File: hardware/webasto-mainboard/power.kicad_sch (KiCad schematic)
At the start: 14 parts, among them U5 BD9G341EFJ

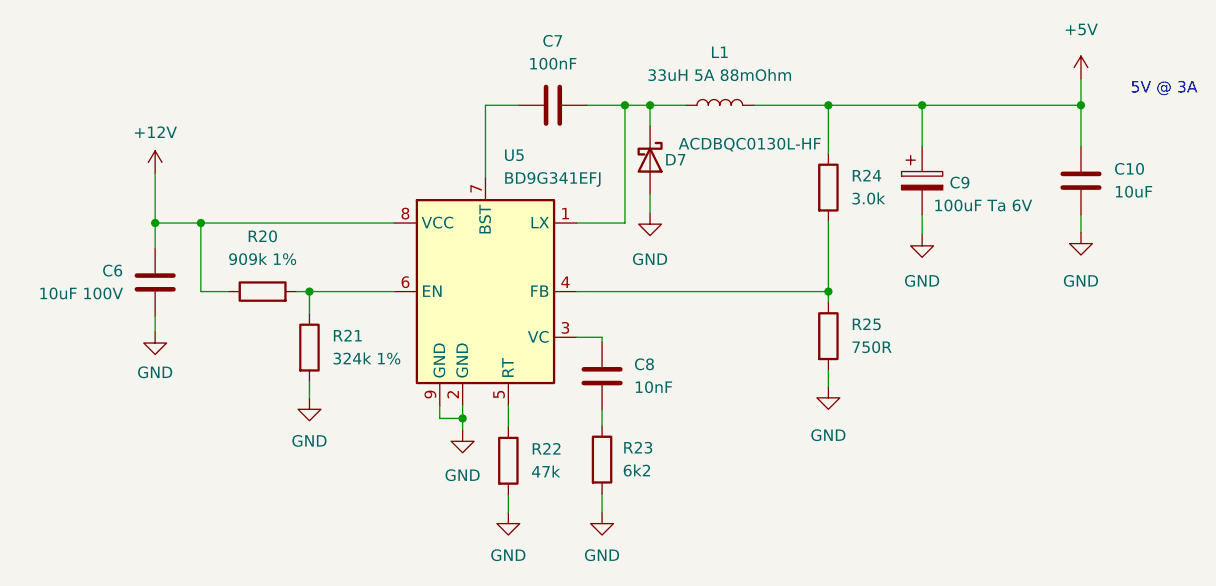
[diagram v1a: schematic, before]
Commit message: Added "USE_USB" input to choose console
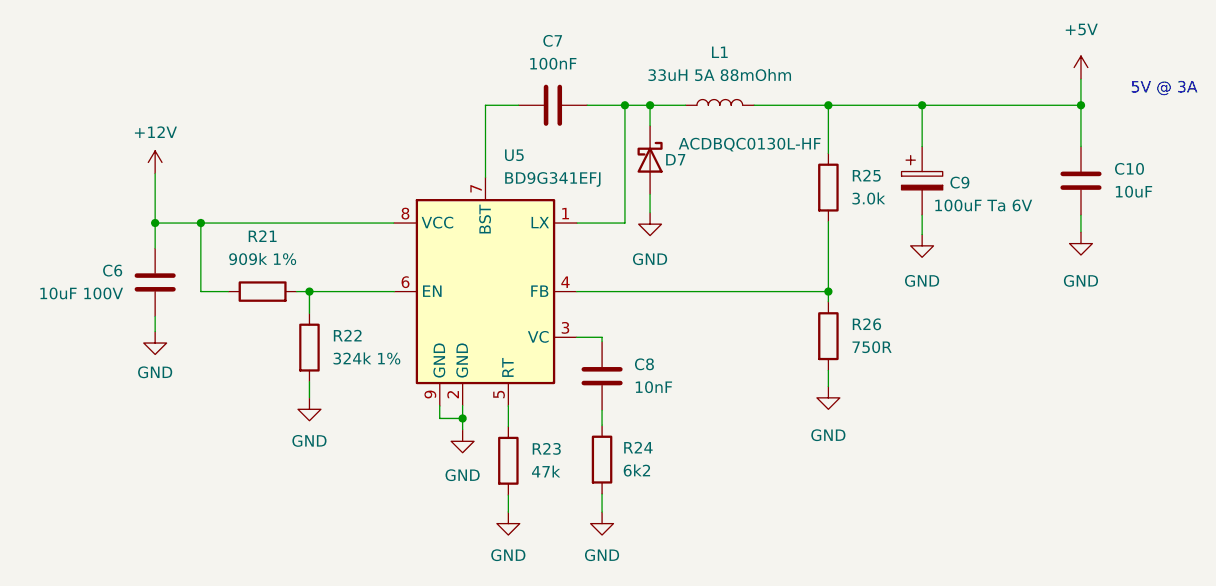
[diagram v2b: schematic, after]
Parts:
- renumbered R20 to R21, R21 to R22, R22 to R23, R23 to R24, R24 to R25, R25 to R26
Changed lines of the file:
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@@
   (symbol (lib_id "Device:R") (at 125.222 86.106 0) (unit 1)
     (in_bom yes) (on_board yes) (fields_autoplaced)
-    (property "Reference" "R21" (id 0) (at 127.762 84.8359 0)
+    (property "Reference" "R22" (id 0) (at 127.762 84.8359 0)
       (effects (font (size 1.27 1.27)) (justify left))
     )
@@
   (symbol (lib_id "power:GND") (at 210.947 73.279 0) (unit 1)
     (in_bom yes) (on_board yes) (fields_autoplaced)
-    (property "Reference" "#PWR056" (id 0) (at 210.947 79.629 0)
+    (property "Reference" "#PWR058" (id 0) (at 210.947 79.629 0)
       (effects (font (size 1.27 1.27)) hide)
     )
@@
   (symbol (lib_id "Device:R") (at 147.32 98.679 0) (unit 1)
     (in_bom yes) (on_board yes) (fields_autoplaced)
-    (property "Reference" "R22" (id 0) (at 149.86 97.4089 0)
+    (property "Reference" "R23" (id 0) (at 149.86 97.4089 0)
       (effects (font (size 1.27 1.27)) (justify left))
     )
@@
   (symbol (lib_id "power:GND") (at 163.068 71.12 0) (unit 1)
     (in_bom yes) (on_board yes) (fields_autoplaced)
-    (property "Reference" "#PWR052" (id 0) (at 163.068 77.47 0)
+    (property "Reference" "#PWR054" (id 0) (at 163.068 77.47 0)
       (effects (font (size 1.27 1.27)) hide)
     )
@@
   (symbol (lib_id "Device:R") (at 182.88 68.326 0) (unit 1)
     (in_bom yes) (on_board yes) (fields_autoplaced)
-    (property "Reference" "R24" (id 0) (at 185.42 67.0559 0)
+    (property "Reference" "R25" (id 0) (at 185.42 67.0559 0)
       (effects (font (size 1.27 1.27)) (justify left))
     )
@@
   (symbol (lib_id "power:GND") (at 193.294 73.533 0) (unit 1)
     (in_bom yes) (on_board yes) (fields_autoplaced)
-    (property "Reference" "#PWR054" (id 0) (at 193.294 79.883 0)
+    (property "Reference" "#PWR056" (id 0) (at 193.294 79.883 0)
       (effects (font (size 1.27 1.27)) hide)
     )
@@
   (symbol (lib_id "Device:R") (at 182.88 84.836 0) (unit 1)
     (in_bom yes) (on_board yes) (fields_autoplaced)
-    (property "Reference" "R25" (id 0) (at 185.42 83.5659 0)
+    (property "Reference" "R26" (id 0) (at 185.42 83.5659 0)
       (effects (font (size 1.27 1.27)) (justify left))
     )
@@
   (symbol (lib_id "power:GND") (at 108.077 84.328 0) (unit 1)
     (in_bom yes) (on_board yes) (fields_autoplaced)
-    (property "Reference" "#PWR047" (id 0) (at 108.077 90.678 0)
+    (property "Reference" "#PWR049" (id 0) (at 108.077 90.678 0)
       (effects (font (size 1.27 1.27)) hide)
     )
@@
   (symbol (lib_id "power:GND") (at 142.24 95.25 0) (unit 1)
     (in_bom yes) (on_board yes) (fields_autoplaced)
-    (property "Reference" "#PWR049" (id 0) (at 142.24 101.6 0)
+    (property "Reference" "#PWR051" (id 0) (at 142.24 101.6 0)
       (effects (font (size 1.27 1.27)) hide)
     )
@@
   (symbol (lib_id "power:GND") (at 125.222 91.694 0) (unit 1)
     (in_bom yes) (on_board yes) (fields_autoplaced)
-    (property "Reference" "#PWR048" (id 0) (at 125.222 98.044 0)
+    (property "Reference" "#PWR050" (id 0) (at 125.222 98.044 0)
       (effects (font (size 1.27 1.27)) hide)
     )
@@
   (symbol (lib_id "power:+12V") (at 108.077 66.802 0) (unit 1)
     (in_bom yes) (on_board yes) (fields_autoplaced)
-    (property "Reference" "#PWR046" (id 0) (at 108.077 70.612 0)
+    (property "Reference" "#PWR048" (id 0) (at 108.077 70.612 0)
       (effects (font (size 1.27 1.27)) hide)
     )
@@
   (symbol (lib_id "power:GND") (at 182.88 90.424 0) (unit 1)
     (in_bom yes) (on_board yes) (fields_autoplaced)
-    (property "Reference" "#PWR053" (id 0) (at 182.88 96.774 0)
+    (property "Reference" "#PWR055" (id 0) (at 182.88 96.774 0)
       (effects (font (size 1.27 1.27)) hide)
     )
@@
   (symbol (lib_id "power:+5V") (at 210.947 56.261 0) (unit 1)
     (in_bom yes) (on_board yes) (fields_autoplaced)
-    (property "Reference" "#PWR055" (id 0) (at 210.947 60.071 0)
+    (property "Reference" "#PWR057" (id 0) (at 210.947 60.071 0)
       (effects (font (size 1.27 1.27)) hide)
     )
@@
   (symbol (lib_id "Device:R") (at 120.015 79.883 90) (unit 1)
     (in_bom yes) (on_board yes) (fields_autoplaced)
-    (property "Reference" "R20" (id 0) (at 120.015 73.787 90))
+    (property "Reference" "R21" (id 0) (at 120.015 73.787 90))
     (property "Value" "909k 1%" (id 1) (at 120.015 76.327 90))
     (property "Footprint" "Resistor_SMD:R_0805_2012Metric_Pad1.20x1.40mm_HandSolder" (id 2) (at 120.015 81.661 90)
@@
   (symbol (lib_id "power:GND") (at 147.32 104.394 0) (unit 1)
     (in_bom yes) (on_board yes) (fields_autoplaced)
-    (property "Reference" "#PWR050" (id 0) (at 147.32 110.744 0)
+    (property "Reference" "#PWR052" (id 0) (at 147.32 110.744 0)
       (effects (font (size 1.27 1.27)) hide)
     )
@@
   (symbol (lib_id "Device:R") (at 157.734 98.552 0) (unit 1)
     (in_bom yes) (on_board yes) (fields_autoplaced)
-    (property "Reference" "R23" (id 0) (at 160.02 97.2819 0)
+    (property "Reference" "R24" (id 0) (at 160.02 97.2819 0)
       (effects (font (size 1.27 1.27)) (justify left))
     )
@@
   (symbol (lib_id "power:GND") (at 157.734 104.394 0) (unit 1)
     (in_bom yes) (on_board yes) (fields_autoplaced)
-    (property "Reference" "#PWR051" (id 0) (at 157.734 110.744 0)
-      (effects (font (size 1.27 1.27)) hide)
-    )
+    (property "Reference" "#PWR053" (id 0) (at 157.734 110.744 0)
+      (effects (font (size 1.27 1.27)) hide)
+    )

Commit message: Added snubbing diodes on all the inputs
- back EMF from relays... I forgot...  so reverse biased diodes from
  GND to signal and from signal to +12V.
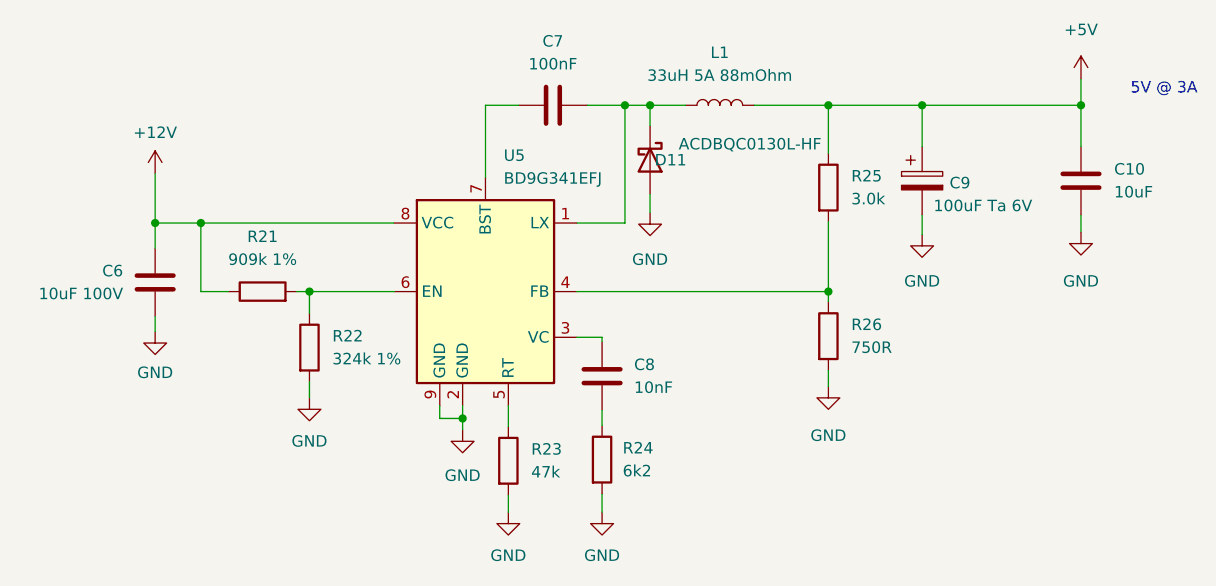
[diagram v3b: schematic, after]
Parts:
- renumbered D7 to D11
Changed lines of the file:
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@@
   (symbol (lib_id "Device:D_Schottky") (at 163.068 65.278 270) (unit 1)
     (in_bom yes) (on_board yes)
-    (property "Reference" "D7" (id 0) (at 167.132 65.278 90)
+    (property "Reference" "D11" (id 0) (at 167.132 65.278 90)
       (effects (font (size 1.27 1.27)) (justify right))
     )
@@
   (symbol (lib_id "power:GND") (at 210.947 73.279 0) (unit 1)
     (in_bom yes) (on_board yes) (fields_autoplaced)
-    (property "Reference" "#PWR058" (id 0) (at 210.947 79.629 0)
+    (property "Reference" "#PWR063" (id 0) (at 210.947 79.629 0)
       (effects (font (size 1.27 1.27)) hide)
     )
@@
   (symbol (lib_id "power:GND") (at 163.068 71.12 0) (unit 1)
     (in_bom yes) (on_board yes) (fields_autoplaced)
-    (property "Reference" "#PWR054" (id 0) (at 163.068 77.47 0)
+    (property "Reference" "#PWR059" (id 0) (at 163.068 77.47 0)
       (effects (font (size 1.27 1.27)) hide)
     )
@@
   (symbol (lib_id "power:GND") (at 193.294 73.533 0) (unit 1)
     (in_bom yes) (on_board yes) (fields_autoplaced)
-    (property "Reference" "#PWR056" (id 0) (at 193.294 79.883 0)
+    (property "Reference" "#PWR061" (id 0) (at 193.294 79.883 0)
       (effects (font (size 1.27 1.27)) hide)
     )
@@
   (symbol (lib_id "power:GND") (at 108.077 84.328 0) (unit 1)
     (in_bom yes) (on_board yes) (fields_autoplaced)
-    (property "Reference" "#PWR049" (id 0) (at 108.077 90.678 0)
+    (property "Reference" "#PWR054" (id 0) (at 108.077 90.678 0)
       (effects (font (size 1.27 1.27)) hide)
     )
@@
   (symbol (lib_id "power:GND") (at 142.24 95.25 0) (unit 1)
     (in_bom yes) (on_board yes) (fields_autoplaced)
-    (property "Reference" "#PWR051" (id 0) (at 142.24 101.6 0)
+    (property "Reference" "#PWR056" (id 0) (at 142.24 101.6 0)
       (effects (font (size 1.27 1.27)) hide)
     )
@@
   (symbol (lib_id "power:GND") (at 125.222 91.694 0) (unit 1)
     (in_bom yes) (on_board yes) (fields_autoplaced)
-    (property "Reference" "#PWR050" (id 0) (at 125.222 98.044 0)
+    (property "Reference" "#PWR055" (id 0) (at 125.222 98.044 0)
       (effects (font (size 1.27 1.27)) hide)
     )
@@
   (symbol (lib_id "power:+12V") (at 108.077 66.802 0) (unit 1)
     (in_bom yes) (on_board yes) (fields_autoplaced)
-    (property "Reference" "#PWR048" (id 0) (at 108.077 70.612 0)
+    (property "Reference" "#PWR053" (id 0) (at 108.077 70.612 0)
       (effects (font (size 1.27 1.27)) hide)
     )
@@
   (symbol (lib_id "power:GND") (at 182.88 90.424 0) (unit 1)
     (in_bom yes) (on_board yes) (fields_autoplaced)
-    (property "Reference" "#PWR055" (id 0) (at 182.88 96.774 0)
+    (property "Reference" "#PWR060" (id 0) (at 182.88 96.774 0)
       (effects (font (size 1.27 1.27)) hide)
     )
@@
   (symbol (lib_id "power:+5V") (at 210.947 56.261 0) (unit 1)
     (in_bom yes) (on_board yes) (fields_autoplaced)
-    (property "Reference" "#PWR057" (id 0) (at 210.947 60.071 0)
+    (property "Reference" "#PWR062" (id 0) (at 210.947 60.071 0)
       (effects (font (size 1.27 1.27)) hide)
     )
@@
   (symbol (lib_id "power:GND") (at 147.32 104.394 0) (unit 1)
     (in_bom yes) (on_board yes) (fields_autoplaced)
-    (property "Reference" "#PWR052" (id 0) (at 147.32 110.744 0)
+    (property "Reference" "#PWR057" (id 0) (at 147.32 110.744 0)
       (effects (font (size 1.27 1.27)) hide)
     )
@@
   (symbol (lib_id "power:GND") (at 157.734 104.394 0) (unit 1)
     (in_bom yes) (on_board yes) (fields_autoplaced)
-    (property "Reference" "#PWR053" (id 0) (at 157.734 110.744 0)
-      (effects (font (size 1.27 1.27)) hide)
-    )
+    (property "Reference" "#PWR058" (id 0) (at 157.734 110.744 0)
+      (effects (font (size 1.27 1.27)) hide)
+    )

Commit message: Update title block on mainboard, print PDFs
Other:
- company: (none) -> Gavin Hurlbut
- title: Webasto Thermo Top C Replacement Controller -> Webasto Replacement Mainboard (Thermo Top C)
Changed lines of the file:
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@@
   (paper "A4")
   (title_block
-    (title "Webasto Thermo Top C Replacement Controller")
-    (date "2023-01-19")
+    (title "Webasto Replacement Mainboard (Thermo Top C)")
+    (date "2023-01-31")
     (rev "v1.0")
+    (company "Gavin Hurlbut")
   )
   (junction (at 210.947 59.182) (diameter 0) (color 0 0 0 0)
